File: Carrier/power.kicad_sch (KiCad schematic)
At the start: 39 parts, among them J8 USB_C_Receptacle_USB2.0_16P, Q1 AO3400A, U10 EL817S1C, U12 USBLC6-2SC6, U2 IP5306

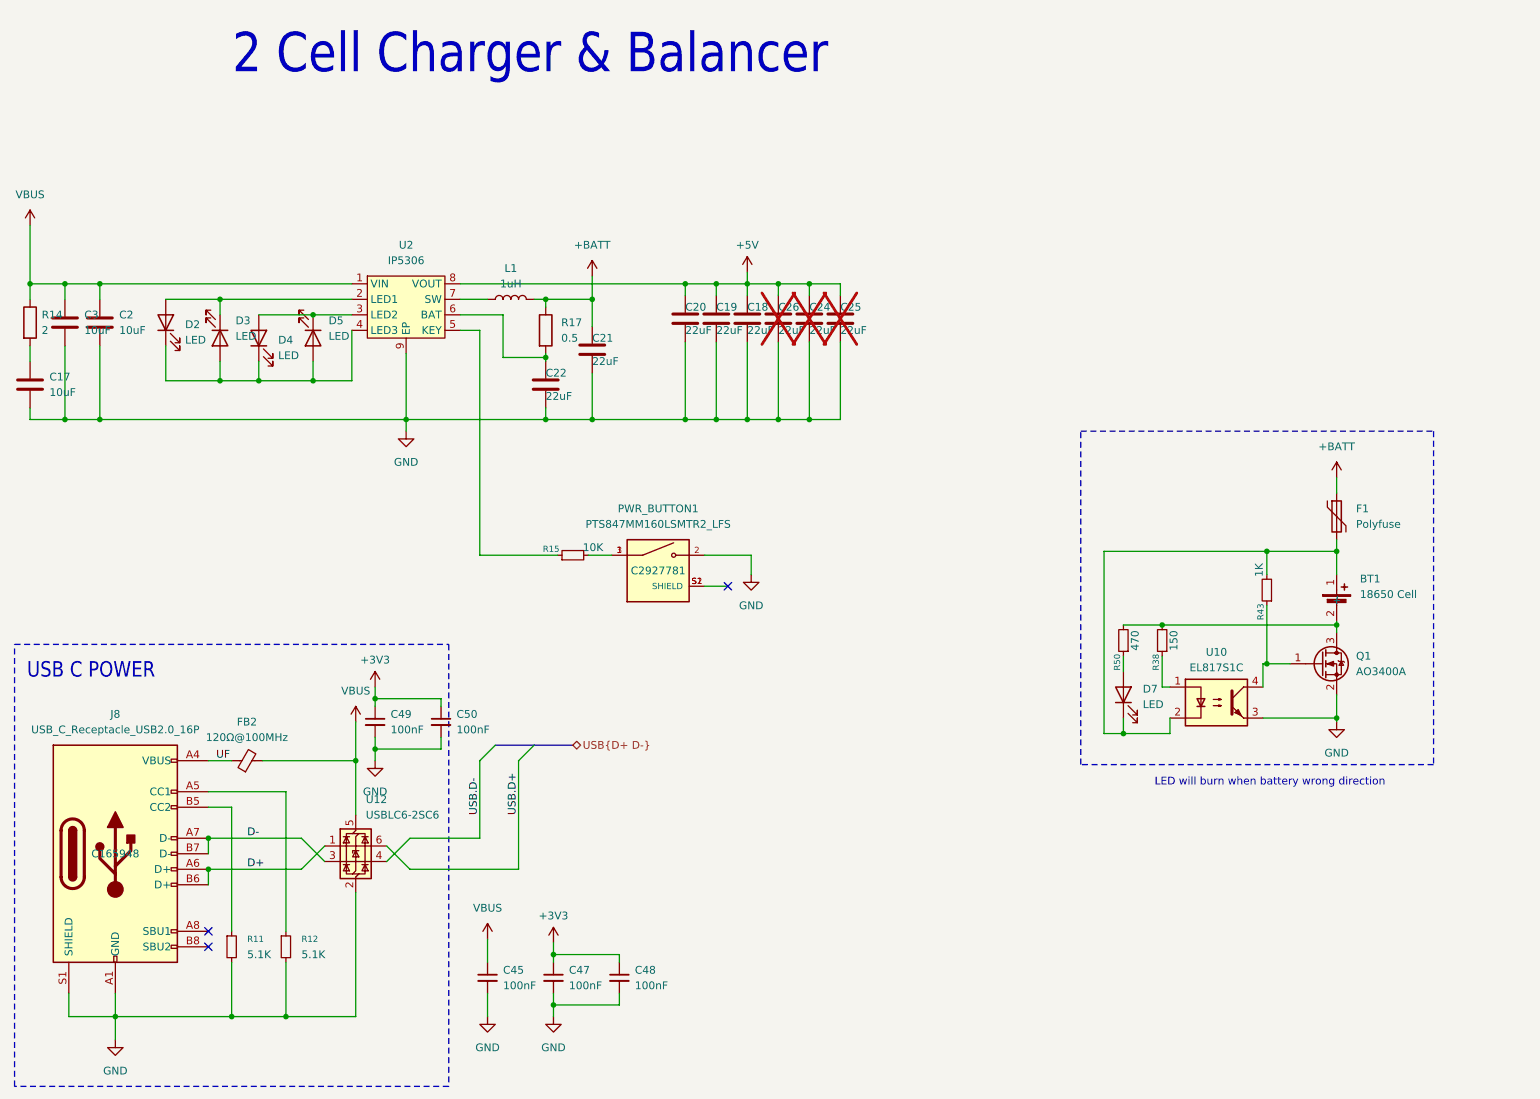
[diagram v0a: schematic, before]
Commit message: Pulled out some stuff I don't need.
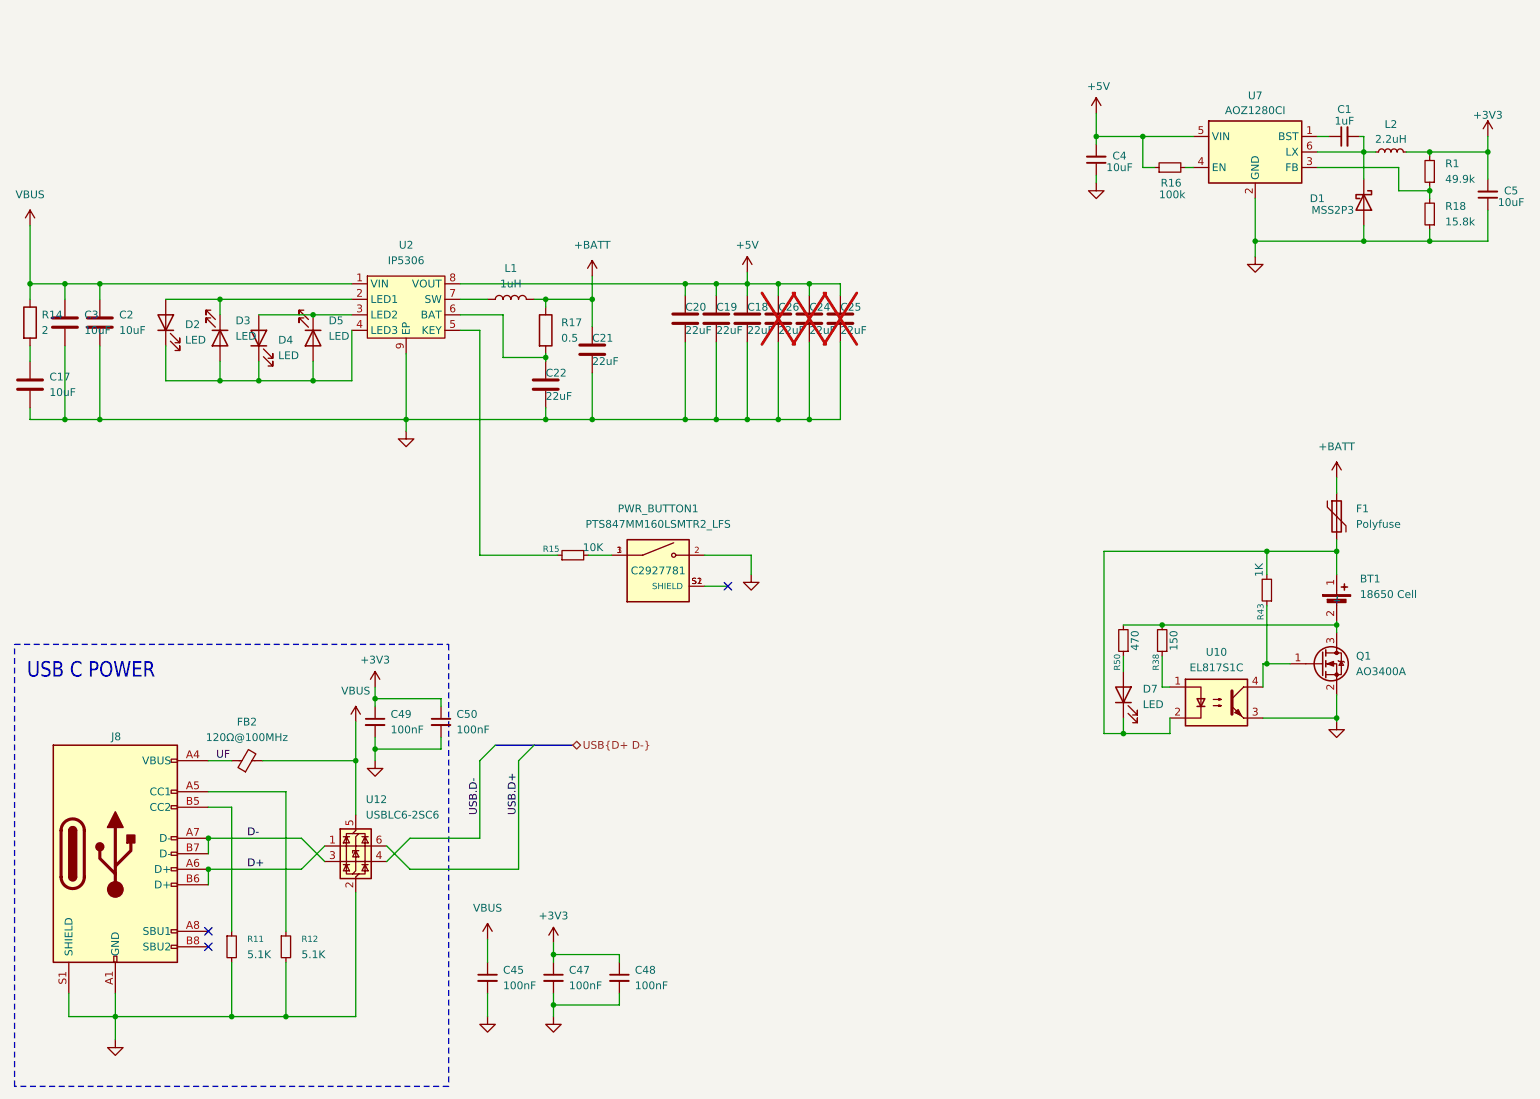
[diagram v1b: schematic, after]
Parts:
- added C1: 1uF, Capacitor_SMD:C_0402_1005Metric, symbol Device:C_Small
- added C4, C5: 10uF, Capacitor_SMD:C_0603_1608Metric, symbol Device:C_Small
- added D1: MSS2P3, Diode_SMD:D_MicroSMP_AK, symbol Device:D_Schottky
- added L2: 2.2uH, Inductor_SMD:L_1008_2520Metric, symbol Device:L_Small
- added R1: 49.9k, Resistor_SMD:R_0402_1005Metric, symbol Device:R_Small
- added R16: 100k, symbol Device:R_Small
- added R18: 15.8k, Resistor_SMD:R_0402_1005Metric, symbol Device:R_Small
- added U7: AOZ1280CI, Package_TO_SOT_SMD:SOT-23-6, symbol Regulator_Switching:AOZ1280CI
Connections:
- net +3V3: now also C5.2, L2.2, R1.2
- net +5V: now also C4.2, R16.1, U7.5 (VIN)
- net GND: now also C4.1, C5.1, D1.2 (A), R18.1, U7.2 (GND)
- new net: C1.1, U7.1 (BST)
- new net: R1.1, R18.2, U7.3 (FB)
- new net: R16.2, U7.4 (EN)
- new net: C1.2, D1.1 (K), L2.1, U7.6 (LX)
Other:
- note removed: "2 Cell Charger & Balancer"
- note removed: "LED will burn when battery wrong direction"
